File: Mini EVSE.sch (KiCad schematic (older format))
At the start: 33 parts, among them IC1 G3MC-201PL DC5, IC2 IRM-03-5, IC3 ATTINY84-20PU, IC4 TMR1-0522, IC5 SI8261BAC-C-IP, J1 RE OUT, J10 M, J2 AC IN, J4 ICP, J5 SWITCH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

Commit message: Moved switch from reset pin as we need reset to be active for simple ISP.
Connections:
- net labels added: MISO, RESET
- net labels removed: PA5, SCK
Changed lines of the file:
@@
 	2650 1750 2750 1650
 Text Label 4450 3450 0    40   ~ 0
-PA5
+MISO
 Text Label 4450 3550 0    40   ~ 0
 CP_OUT
 Text Label 2850 1650 0    40   ~ 0
-PA5
+MISO
 Text Label 3750 1750 0    40   ~ 0
 CP_OUT
 Text Label 4450 3350 0    40   ~ 0
-SCK
+SW
 Text Label 2850 1750 0    40   ~ 0
-SCK
+SW
 Text Label 4450 4150 0    40   ~ 0
-SW
+RESET
 Text Label 2850 1850 0    40   ~ 0
-SW
+RESET
 Text Label 4450 3850 0    40   ~ 0
 XTAL1

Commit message: Started working on three-phase setup
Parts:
- removed IC1: G3MC-201PL DC5, Miscellaneous:SIP4_Omron-SSR_Pitch10.16mm_Straight, symbol S102S01
- removed IC3: ATTINY84-20PU, Housings_DIP:DIP-14_W7.62mm_LongPads, symbol ATTINY84-20PU
- removed J1: RE OUT, Connectors_Terminal_Blocks:TerminalBlock_Pheonix_MKDS1.5-2pol, symbol CONN_01X02_MALE
- removed J2: AC IN, Connectors_Terminal_Blocks:TerminalBlock_Pheonix_MKDS1.5-2pol, symbol CONN_01X02_MALE
- removed R10: 301, Miscellaneous:R_Axial_DIN0207_L6.3mm_D2.5mm_P10.16mm_Horizontal, symbol R
- added C?: C_Small, symbol C_Small
- added D? (x4): D_Schottky, symbol D_Schottky
- added IC3: ATMEGA328PB-AU, Housings_QFP:TQFP-32_7x7mm_Pitch0.8mm, symbol ATMEGA328PB-AU
- added J2: AC IN, symbol CONN_01X04
- added J3: AC OUT, symbol CONN_01X04
- added R? (x2): 100k, symbol R
- added R?: R, symbol R
- added R? (x4): 10k, symbol R
- added RL1, RL2, RL3, RL4: ADJH21005, Relays_THT:Relay_SPST-NO_OMRON-G5Q, symbol ADJH21005
- added U? (x2): BD6211F-E2, symbol BD6211F-E2
- added U?: H11AA1, Housings_DIP:DIP-6_W7.62mm_SMD, symbol H11AA1
- added U? (x2): 74LVC2G04, symbol 74LVC2G04
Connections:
- net labels added: +5C, L1-IN, L1-OUT, L2-IN, L2-OUT, L3-IN, L3-OUT, MOSI, N-IN, N-OUT, N_MEAS, OFF12, OFF34, ON12, ON34, RXD, SCK, TXD
- wire segments 99 -> 239
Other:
- moved on the sheet: C1, C2, C3, C4, C5, D1, D2, F1, IC2, IC4, IC5, J10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

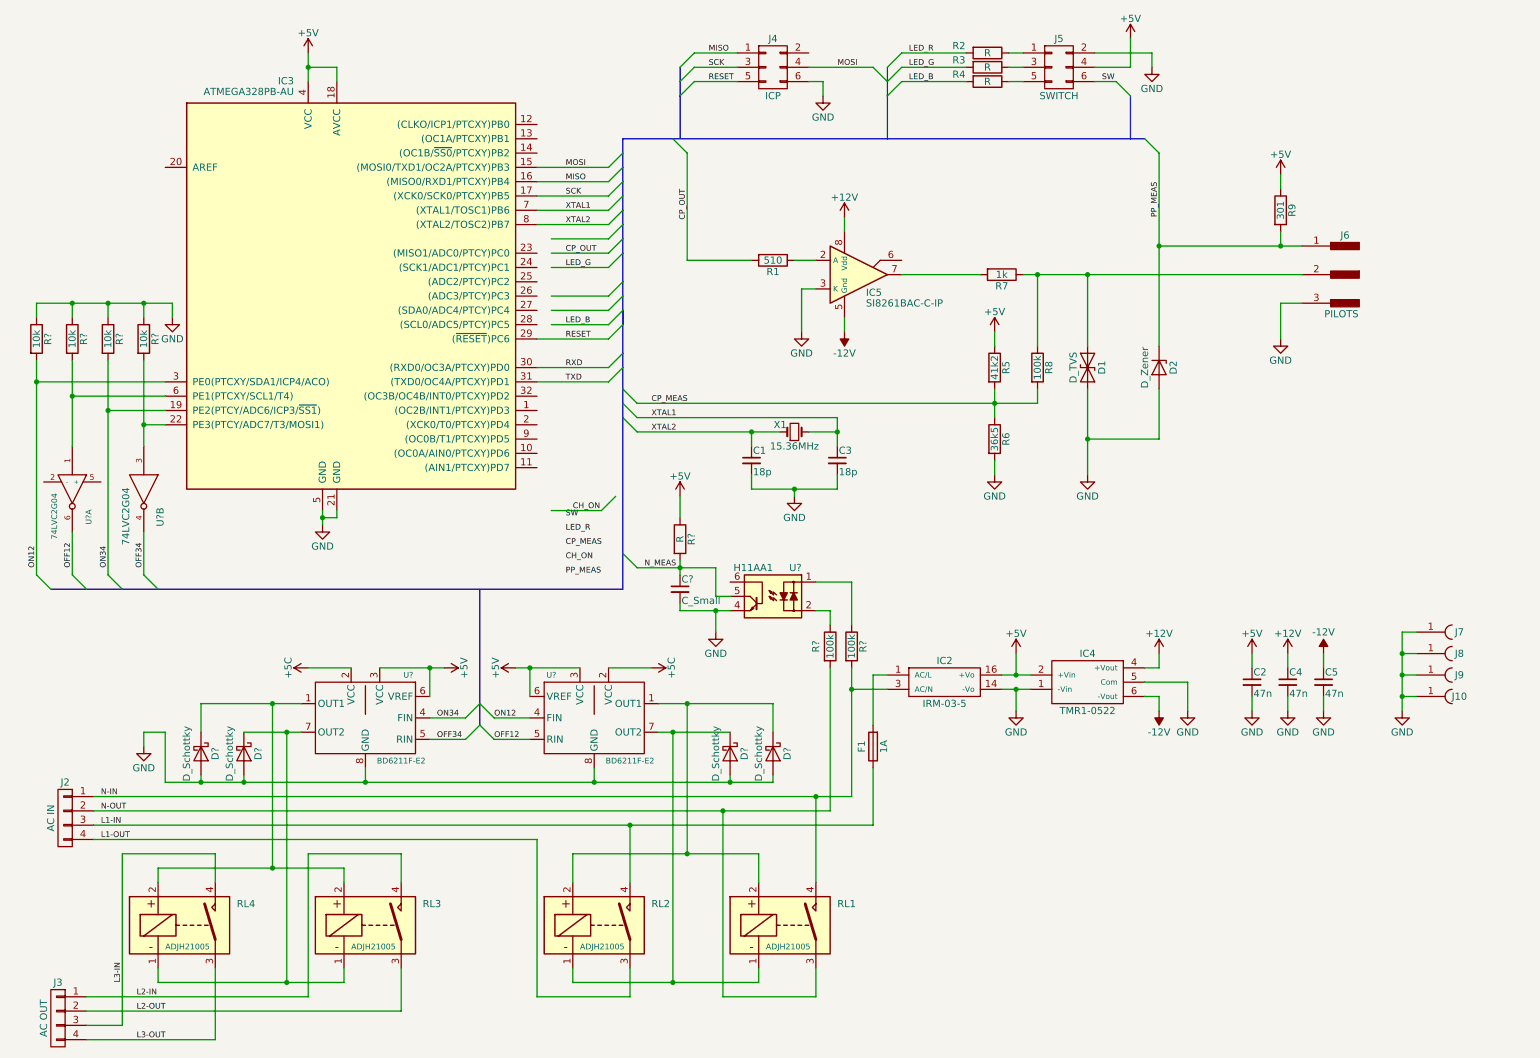
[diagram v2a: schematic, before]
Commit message: Working on 3-phase version - asssigned all MCU pins
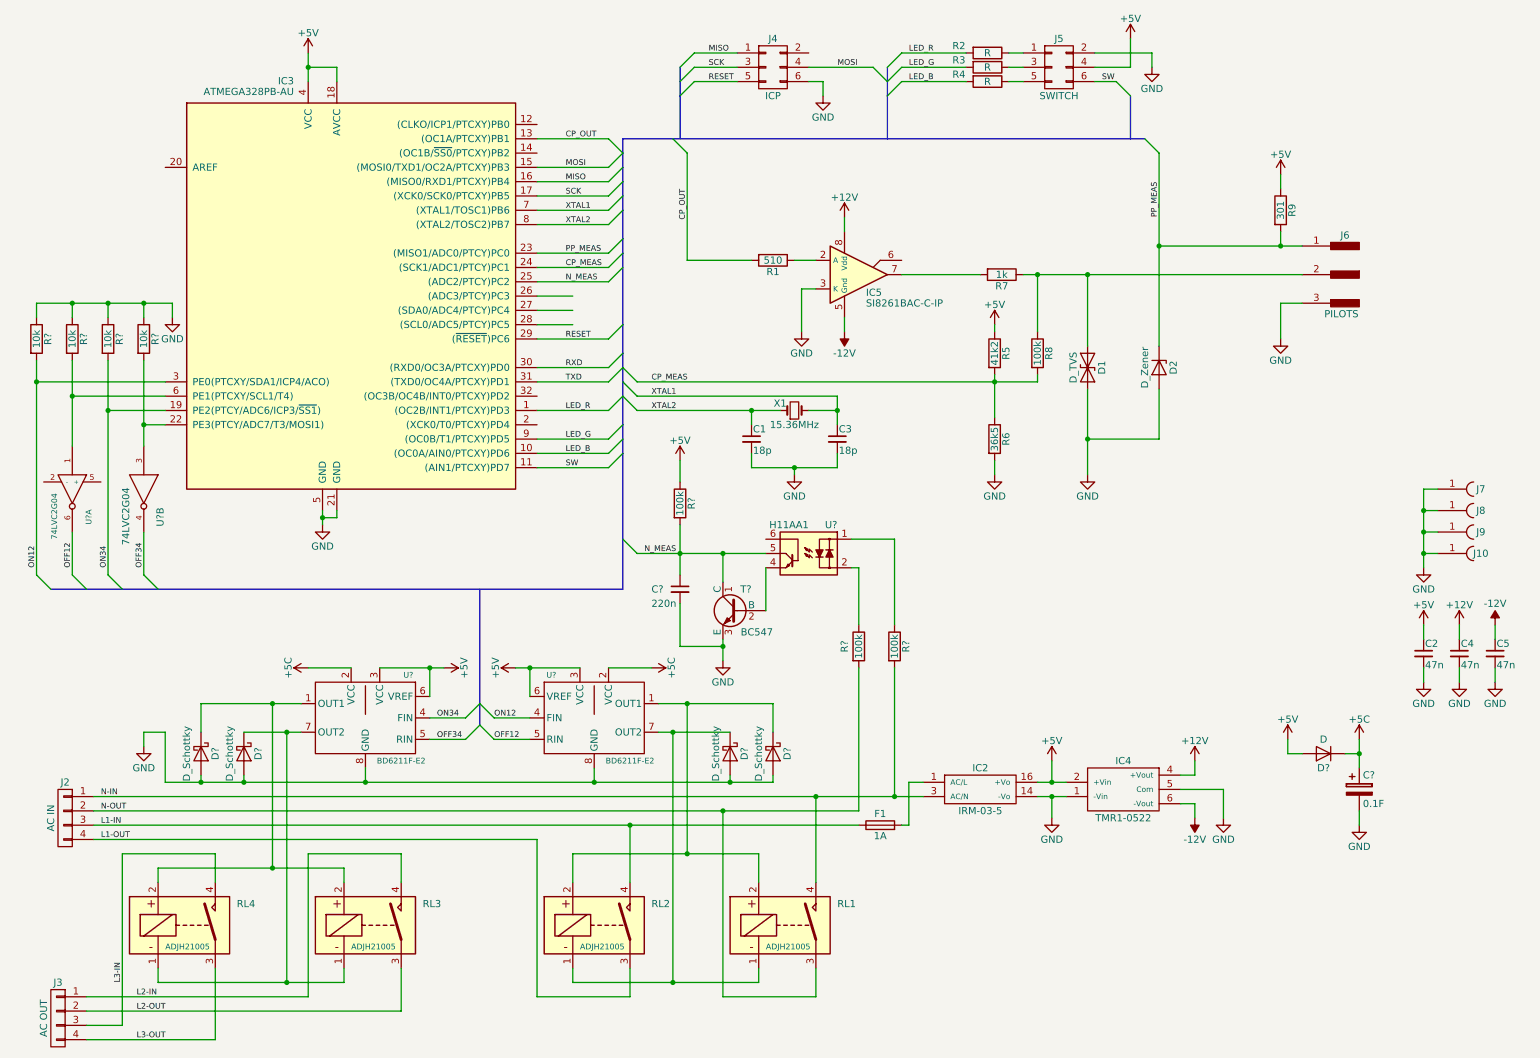
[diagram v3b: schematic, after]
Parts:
- added C?: 0.1F, symbol CP
- added D?: D, symbol D
- added T?: BC547, TO_SOT_Packages_THT:TO-92_Molded_Narrow, symbol BC547
- C?: value C_Small -> 220n
- R?: value R -> 100k
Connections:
- net labels removed: CH_ON
- wire segments 239 -> 249
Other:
- moved on the sheet: C1, C2, C3, C4, C5, F1, IC2, IC4, J10, J7, J8, J9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

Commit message: Various improvements
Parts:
- gave numbers to parts that had none: 1
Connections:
- net +5C: now also IC?.5 (+), U?.3 (VCC), U?.3 (VCC), U?.6 (VREF), U?.6 (VREF)
- net +5V: no longer U?.3 (VCC), U?.3 (VCC), U?.6 (VREF), U?.6 (VREF)
- net GND: now also IC?.2 (-)
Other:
- moved on the sheet: IC?A, R?
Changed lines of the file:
@@
 Wire Wire Line
 	2400 5350 2600 5350
-Wire Wire Line
-	3150 5100 3500 5100
-Wire Wire Line
-	3500 5100 3600 5100
-Wire Wire Line
-	4100 5100 4200 5100
-Wire Wire Line
-	4200 5100 4550 5100
-$Comp
-L +5V #PWR?
-U 1 1 5B65FE4B
-P 3600 5100
-F 0 "#PWR?" H 3600 4950 50  0001 C CNN
-F 1 "+5V" H 3600 5240 50  0000 C CNN
-F 2 "" H 3600 5100 50  0001 C CNN
-F 3 "" H 3600 5100 50  0001 C CNN
-	1    3600 5100
-	0    1    1    0
-$EndComp
-Connection ~ 3500 5100
-Connection ~ 4200 5100
-Wire Bus Line
-	850  4550 1100 4550
-Wire Bus Line
-	1100 4550 1350 4550
-Wire Bus Line
-	1350 4550 1600 4550
-Wire Bus Line
-	1600 4550 4850 4550
+Wire Bus Line
+	4850 4550 1600 4550
+Wire Bus Line
+	1600 4550 1350 4550
+Wire Bus Line
+	1350 4550 1050 4550
+Wire Bus Line
+	1050 4550 750  4550
 Wire Bus Line
 	3850 4550 3850 5350
@@
 L +5C #PWR?
 U 1 1 5B6B2B21
-P 2650 5100
-F 0 "#PWR?" H 2650 4950 50  0001 C CNN
-F 1 "+5C" H 2650 5240 50  0000 C CNN
-F 2 "" H 2650 5100 50  0001 C CNN
-F 3 "" H 2650 5100 50  0001 C CNN
-	1    2650 5100
-	0    -1   -1   0
-$EndComp
-Wire Wire Line
-	2650 5100 2950 5100
+P 2950 4900
+F 0 "#PWR?" H 2950 4750 50  0001 C CNN
+F 1 "+5C" H 2950 5040 50  0000 C CNN
+F 2 "" H 2950 4900 50  0001 C CNN
+F 3 "" H 2950 4900 50  0001 C CNN
+	1    2950 4900
+	1    0    0    -1
+$EndComp
+Wire Wire Line
+	2950 4900 2950 5000
+Wire Wire Line
+	2950 5000 2950 5100
 $Comp
 L +5C #PWR?
 U 1 1 5B6B2D46
-P 5050 5100
-F 0 "#PWR?" H 5050 4950 50  0001 C CNN
-F 1 "+5C" H 5050 5240 50  0000 C CNN
-F 2 "" H 5050 5100 50  0001 C CNN
-F 3 "" H 5050 5100 50  0001 C CNN
-	1    5050 5100
-	0    1    1    0
-$EndComp
-Wire Wire Line
-	5050 5100 4750 5100
-$Comp
-L 74LVC2G04 U?
+P 4750 4900
+F 0 "#PWR?" H 4750 4750 50  0001 C CNN
+F 1 "+5C" H 4750 5040 50  0000 C CNN
+F 2 "" H 4750 4900 50  0001 C CNN
+F 3 "" H 4750 4900 50  0001 C CNN
+	1    4750 4900
+	1    0    0    -1
+$EndComp
+Wire Wire Line
+	4750 4900 4750 5000
+Wire Wire Line
+	4750 5000 4750 5100
+$Comp
+L 74LVC2G04 IC?
 U 1 1 5B6B4079
-P 1000 3850
-F 0 "U?" H 1195 3965 40  0000 C CNN
-F 1 "74LVC2G04" H 1190 3725 40  0000 C CNN
-F 2 "" H 1000 3850 50  0001 C CNN
-F 3 "" H 1000 3850 50  0001 C CNN
-	1    1000 3850
-	0    1    1    0
-$EndComp
-Entry Wire Line
-	750  4450 850  4550
-$Comp
-L 74LVC2G04 U?
+P 950 3850
+F 0 "IC?" H 1000 3950 40  0000 C CNN
+F 1 "74LVC2G04" H 600 3750 40  0000 C CNN
+F 2 "" H 950 3850 50  0001 C CNN
+F 3 "" H 950 3850 50  0001 C CNN
+	1    950  3850
+	0    -1   1    0
+$EndComp
+Entry Wire Line
+	650  4450 750  4550
+$Comp
+L 74LVC2G04 IC?
 U 2 1 5B6B4675
 P 1500 3850
-F 0 "U?" H 1695 3965 50  0000 C CNN
-F 1 "74LVC2G04" H 1690 3725 50  0000 C CNN
+F 0 "IC?" H 1550 3950 40  0000 C CNN
+F 1 "74LVC2G04" H 1690 3725 40  0000 C CNN
 F 2 "" H 1500 3850 50  0001 C CNN
 F 3 "" H 1500 3850 50  0001 C CNN
@@
 Entry Wire Line
 	1250 4450 1350 4550
-$Comp
-L +5V #PWR?
-U 1 1 5B6B4AED
-P 4100 5100
-F 0 "#PWR?" H 4100 4950 50  0001 C CNN
-F 1 "+5V" H 4100 5240 50  0000 C CNN
-F 2 "" H 4100 5100 50  0001 C CNN
-F 3 "" H 4100 5100 50  0001 C CNN
-	1    4100 5100
-	0    -1   -1   0
-$EndComp
-Wire Wire Line
-	3500 5300 3500 5100
-Wire Wire Line
-	4200 5300 4200 5100
-Wire Wire Line
-	750  2950 750  3100
-Wire Wire Line
-	750  3100 750  4450
-Wire Wire Line
-	750  3100 1650 3100
+Wire Wire Line
+	650  2950 650  3100
+Wire Wire Line
+	650  3100 650  4450
+Wire Wire Line
+	650  3100 1650 3100
 Wire Wire Line
 	1650 3300 1250 3300
@@
 	1650 3400 1500 3400
 Wire Wire Line
-	1650 3200 1000 3200
-Entry Wire Line
-	1000 4450 1100 4550
+	1650 3200 950  3200
+Entry Wire Line
+	950  4450 1050 4550
 Entry Wire Line
 	1500 4450 1600 4550
-Connection ~ 750  3100
-Connection ~ 1000 3200
+Connection ~ 650  3100
+Connection ~ 950  3200
 Connection ~ 1250 3300
 Connection ~ 1500 3400
@@
 L R R?
 U 1 1 5B6B7738
-P 750 2800
-F 0 "R?" V 830 2800 50  0000 C CNN
-F 1 "10k" V 750 2800 50  0000 C CNN
-F 2 "" V 680 2800 50  0001 C CNN
-F 3 "" H 750 2800 50  0001 C CNN
-	1    750  2800
+P 650 2800
+F 0 "R?" V 730 2800 50  0000 C CNN
+F 1 "10k" V 650 2800 50  0000 C CNN
+F 2 "" V 580 2800 50  0001 C CNN
+F 3 "" H 650 2800 50  0001 C CNN
+	1    650  2800
 	1    0    0    -1
 $EndComp
@@
 L R R?
 U 1 1 5B6B77FB
-P 1000 2800
-F 0 "R?" V 1080 2800 50  0000 C CNN
-F 1 "10k" V 1000 2800 50  0000 C CNN
-F 2 "" V 930 2800 50  0001 C CNN
-F 3 "" H 1000 2800 50  0001 C CNN
-	1    1000 2800
+P 950 2800
+F 0 "R?" V 1030 2800 50  0000 C CNN
+F 1 "10k" V 950 2800 50  0000 C CNN
+F 2 "" V 880 2800 50  0001 C CNN
+F 3 "" H 950 2800 50  0001 C CNN
+	1    950  2800
 	1    0    0    -1
 $EndComp
@@
 $EndComp
 Wire Wire Line
-	750  2650 750  2550
-Wire Wire Line
-	750  2550 1000 2550
-Wire Wire Line
-	1000 2550 1250 2550
+	650  2650 650  2550
+Wire Wire Line
+	650  2550 950  2550
+Wire Wire Line
+	950  2550 1250 2550
 Wire Wire Line
 	1250 2550 1500 2550
@@
 	1500 2550 1500 2650
 Wire Wire Line
-	1000 2650 1000 2550
-Connection ~ 1000 2550
+	950  2650 950  2550
+Connection ~ 950  2550
 Wire Wire Line
 	1250 2650 1250 2550
@@
 Connection ~ 1500 2550
 Wire Wire Line
-	1000 2950 1000 3200
-Wire Wire Line
-	1000 3200 1000 3550
-Wire Wire Line
-	1000 4450 1000 4150
+	950  2950 950  3200
+Wire Wire Line
+	950  3200 950  3550
+Wire Wire Line
+	950  4450 950  4150
 Wire Wire Line
 	1500 4450 1500 4150
@@
 Wire Wire Line
 	1500 3400 1500 3550
-Text Label 750  4400 1    40   ~ 0
+Text Label 650  4400 1    40   ~ 0
 ON12
-Text Label 1000 4400 1    40   ~ 0
+Text Label 950  4400 1    40   ~ 0
 OFF12
 Text Label 1250 4400 1    40   ~ 0
@@
 	4750 3700 4850 3600
 Wire Bus Line
-	4850 4550 4850 4200
-Wire Bus Line
-	4850 4200 4850 3600
-Wire Bus Line
-	4850 3600 4850 3500
-Wire Bus Line
-	4850 3500 4850 3400
-Wire Bus Line
-	4850 3400 4850 3200
-Wire Bus Line
-	4850 3200 4850 3100
-Wire Bus Line
-	4850 3100 4850 3000
-Wire Bus Line
-	4850 3000 4850 2900
-Wire Bus Line
-	4850 2900 4850 2700
-Wire Bus Line
-	4850 2700 4850 2200
-Wire Bus Line
-	4850 2200 4850 2100
-Wire Bus Line
-	4850 2100 4850 1900
-Wire Bus Line
-	4850 1900 4850 1800
-Wire Bus Line
-	4850 1800 4850 1700
-Wire Bus Line
-	4850 1700 4850 1600
-Wire Bus Line
-	4850 1600 4850 1500
-Wire Bus Line
-	4850 1500 4850 1400
+	4850 1400 4850 1500
+Wire Bus Line
+	4850 1500 4850 1600
+Wire Bus Line
+	4850 1600 4850 1700
+Wire Bus Line
+	4850 1700 4850 1800
+Wire Bus Line
+	4850 1800 4850 1900
+Wire Bus Line
+	4850 1900 4850 2100
+Wire Bus Line
+	4850 2100 4850 2200
+Wire Bus Line
+	4850 2200 4850 2300
+Wire Bus Line
+	4850 2300 4850 2700
+Wire Bus Line
+	4850 2700 4850 2900
+Wire Bus Line
+	4850 2900 4850 3000
+Wire Bus Line
+	4850 3000 4850 3100
+Wire Bus Line
+	4850 3100 4850 3200
+Wire Bus Line
+	4850 3200 4850 3400
+Wire Bus Line
+	4850 3400 4850 3500
+Wire Bus Line
+	4850 3500 4850 3600
+Wire Bus Line
+	4850 3600 4850 4200
+Wire Bus Line
+	4850 4200 4850 4550
 Entry Wire Line
 	4750 2400 4850 2300
 Text Label 4450 2400 0    40   ~ 0
 N_MEAS
+Wire Wire Line
+	2950 5000 3150 5000
+Wire Wire Line
+	3150 5000 3550 5000
+Wire Wire Line
+	3150 5000 3150 5100
+Connection ~ 2950 5000
+Wire Wire Line
+	3500 5300 3550 5300
+Wire Wire Line
+	3550 5300 3550 5000
+Connection ~ 3150 5000
+Wire Wire Line
+	4550 5100 4550 5000
+Wire Wire Line
+	4150 5000 4550 5000
+Wire Wire Line
+	4550 5000 4750 5000
+Connection ~ 4750 5000
+Wire Wire Line
+	4200 5300 4150 5300
+Wire Wire Line
+	4150 5300 4150 5000
+Connection ~ 4550 5000
+$Comp
+L GND #PWR?
+U 1 1 5BBE5800
+P 1150 4000
+F 0 "#PWR?" H 1150 3750 50  0001 C CNN
+F 1 "GND" H 1150 3850 50  0000 C CNN
+F 2 "" H 1150 4000 50  0001 C CNN
+F 3 "" H 1150 4000 50  0001 C CNN
+	1    1150 4000
+	1    0    0    -1
+$EndComp
+$Comp
+L +5C #PWR?
+U 1 1 5BBE620E
+P 750 3600
+F 0 "#PWR?" H 750 3450 50  0001 C CNN
+F 1 "+5C" H 750 3740 50  0000 C CNN
+F 2 "" H 750 3600 50  0001 C CNN
+F 3 "" H 750 3600 50  0001 C CNN
+	1    750  3600
+	1    0    0    -1
+$EndComp
+Wire Wire Line
+	750  3600 750  3800
+Wire Wire Line
+	1150 3800 1150 4000
 $EndSCHEMATC
